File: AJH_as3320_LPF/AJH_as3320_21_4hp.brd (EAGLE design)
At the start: 19 x 106.8 mm, 58 parts, among them IC1 TL072D, IC2 CEM3320QFN24, IC3 LM4040 5.0V, IC4 TL074D, J1 PJ301_THONKICONN6, J2 PJ301_THONKICONN6, J3 PJ301_THONKICONN6, J4 PJ301_THONKICONN6

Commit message: Maded Multisheet and added input buffer
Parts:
- IC1: value TL072D -> TL074D; device linear:SO08 -> linear:SO14
- moved C11 134.6 mm to (5.59, -34.9)
- moved D2 127.7 mm to (1.27, -24.6), turned to 0 degrees
- moved R23 124.2 mm to (11.6, -24.5)
- moved D1 120.3 mm to (13.1, -17.1), turned to 0 degrees
- moved IC3 114.5 mm to (1.02, -18.0), turned to 0 degrees
- moved JP1 111.5 mm to (2.03, -7.87), turned to 0 degrees
- moved C2 107.5 mm to (0.13, -30.0), turned to 0 degrees
- moved C14 102.7 mm to (13.1, -5.21), turned to 0 degrees
- moved C13 102.5 mm to (7.49, -5.21), turned to 0 degrees
- moved C1 101.9 mm to (16.0, -24.3), turned to 0 degrees
- moved C3 87.9 mm to (5.59, -30.0)
- moved C4 81.2 mm to (11.0, -30.0)
- moved C6 74.6 mm to (0.13, -34.9), turned to 0 degrees
- moved C5 68.7 mm to (16.5, -30.0), turned to 0 degrees
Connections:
- new net N$9: IC1.10, J2.P3
- new net V+: IC1.4, IC4.4
- new net V-: IC1.11, IC4.11
- net -12V: no longer IC1.4, IC4.11
- net 12V: no longer IC1.8, IC4.4
- net LOWPASS_IN: now also IC1.8, IC1.9; no longer J2.P3
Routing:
- net 12V: track 115.0 -> 1.62 mm, vias 6 -> 0
- net -12V: track 141.4 -> 31.2 mm, vias 5 -> 3
- net N$1: track 4.84 -> 22.4 mm
- net GND: track 94.6 -> 87.2 mm
- net -5VIN: track 25.4 -> 19.6 mm
- net N$20: track 5.50 -> 0.00 mm
- net LOWPASS_OUT: track 30.4 -> 35.6 mm
- net N$6: track 5.07 -> 0.00 mm
- net N$7: track 61.9 -> 64.8 mm
- net N$8: track 4.95 -> 6.75 mm
- net LOWPASS_IN: track 31.1 -> 29.3 mm

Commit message: Updated power to op-amps
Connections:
- removed net V+: IC1.4, IC4.4
- removed net V-: IC1.11, IC4.11
- net -12V: now also IC1.11, IC4.11
- net 12V: now also IC1.4, IC4.4
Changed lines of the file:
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@@
 <contactref element="C1" pad="1"/>
 <contactref element="C13" pad="+"/>
+<contactref element="IC1" pad="4"/>
+<contactref element="IC4" pad="4"/>
+<wire x1="6.491" y1="53.792" x2="7.052" y2="77.597" width="0" layer="19" extent="1-1"/>
+<wire x1="10.672" y1="36.003" x2="6.491" y2="53.792" width="0" layer="19" extent="1-1"/>
 <wire x1="9.093" y1="-5.207" x2="10.672" y2="34.381" width="0" layer="19" extent="1-1"/>
 <wire x1="11.181" y1="-17.145" x2="9.093" y2="-5.207" width="0" layer="19" extent="1-1"/>
@@
 <contactref element="C14" pad="-"/>
 <contactref element="R23" pad="1"/>
-<wire x1="0.977" y1="-29.972" x2="0.977" y2="-34.925" width="0" layer="19" extent="1-1"/>
-<wire x1="3.17" y1="-24.638" x2="0.977" y2="-29.972" width="0" layer="19" extent="1-1"/>
-<wire x1="10.707" y1="-24.511" x2="3.17" y2="-24.638" width="0" layer="19" extent="1-1"/>
+<contactref element="IC1" pad="11"/>
+<contactref element="IC4" pad="11"/>
+<wire x1="11.691" y1="53.792" x2="12.252" y2="77.597" width="0" layer="19" extent="1-1"/>
+<wire x1="11.469" y1="37.631" x2="11.691" y2="53.792" width="0" layer="19" extent="1-1"/>
+<wire x1="11.481" y1="-5.207" x2="3.175" y2="28.2614" width="0" layer="19" extent="1-1"/>
+<wire x1="10.707" y1="-24.511" x2="11.481" y2="-5.207" width="0" layer="19" extent="1-1"/>
 <wire x1="11.899" y1="-29.972" x2="10.707" y2="-24.511" width="0" layer="19" extent="1-1"/>
-<wire x1="11.481" y1="-5.207" x2="10.707" y2="-24.511" width="0" layer="19" extent="1-1"/>
-<wire x1="3.175" y1="28.2614" x2="11.481" y2="-5.207" width="0" layer="19" extent="1-1"/>
+<wire x1="3.17" y1="-24.638" x2="10.707" y2="-24.511" width="0" layer="19" extent="1-1"/>
+<wire x1="0.977" y1="-29.972" x2="3.17" y2="-24.638" width="0" layer="19" extent="1-1"/>
+<wire x1="0.977" y1="-34.925" x2="0.977" y2="-29.972" width="0" layer="19" extent="1-1"/>
 </signal>
 <signal name="N$82">
@@
 <wire x1="6.071" y1="13.589" x2="4.674" y2="12.192" width="0.2032" layer="16"/>
 </signal>
-<signal name="V+">
-<contactref element="IC1" pad="4"/>
-<contactref element="IC4" pad="4"/>
-<wire x1="6.491" y1="53.792" x2="7.052" y2="77.597" width="0" layer="19" extent="1-1"/>
-</signal>
-<signal name="V-">
-<contactref element="IC1" pad="11"/>
-<contactref element="IC4" pad="11"/>
-<wire x1="11.691" y1="53.792" x2="12.252" y2="77.597" width="0" layer="19" extent="1-1"/>
-</signal>
 <signal name="N$6">

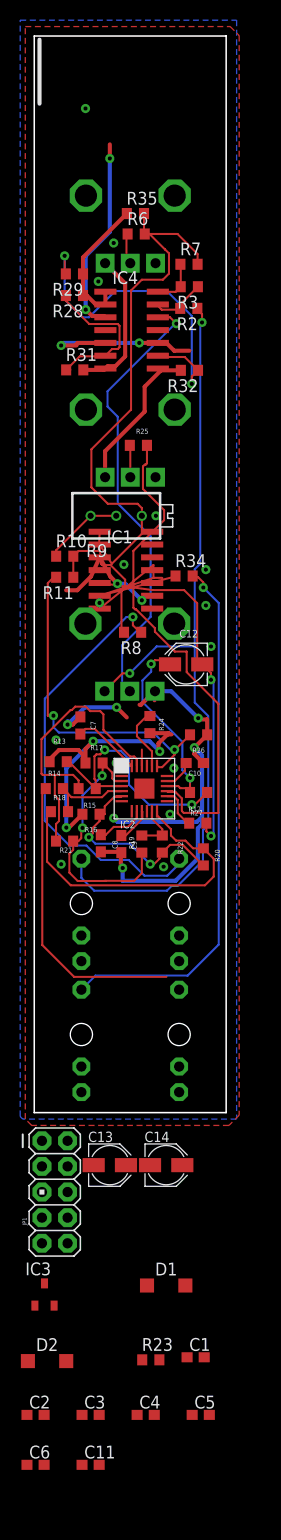
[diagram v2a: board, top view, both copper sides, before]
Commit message: First Bandpass Circuit
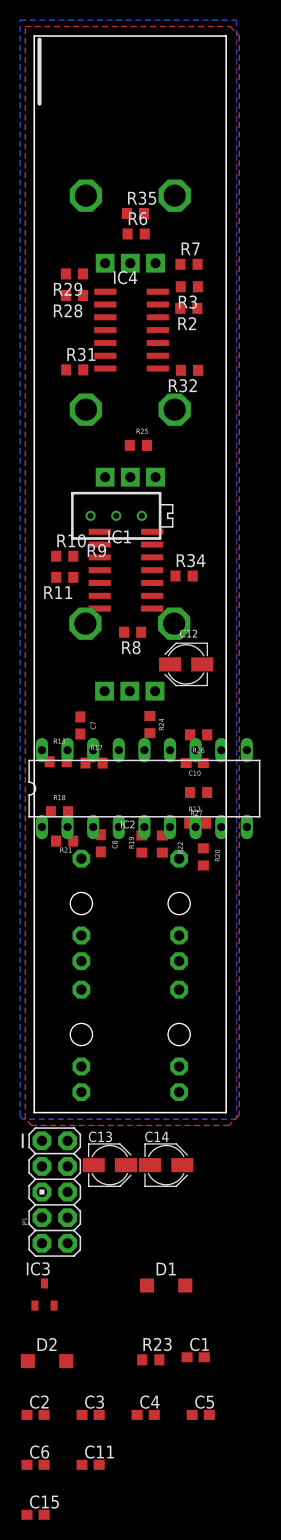
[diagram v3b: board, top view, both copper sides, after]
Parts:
- removed C9: 300pF, rcl:C0603
- removed R14, R15: 91k, rcl:R0603
- removed R16: 220k, rcl:R0603
- added C15: 300pF, rcl:C0603
- IC2: value CEM3320QFN24 -> CEM3320; device CEM:QFN24 -> CEM:DIL18
- R25: value 49.9k -> 68K
- renumbered J1 to FM_IN, J2 to SIGNALIN, J3 to V-OCT, J4 to OUTPUT
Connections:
- net LOWPASS_OUT renamed BANDPASS_OUT
- removed net LOWPASS_IN: IC1.8, IC1.9, R14.2
- removed net N$41: C8.2, IC2.P$8
- removed net N$42: C9.2, IC2.P$9
- removed net N$45: IC2.P$4, R14.1, R18.1
- removed net N$46: IC2.P$12, R18.2, R20.2
- removed net N$47: IC2.P$11, R19.1, R22.2
- removed net N$49: IC2.P$23, R15.1, R21.1
- removed net N$50: C12.+, IC2.P$16, R12.1
- removed net N$52: IC2.P$5, R16.2, R20.1, R22.1
- removed net N$53: IC2.P$2, R17.1, R19.2, R21.2
- new net BANDPASS_IN: C15.1, IC1.8, IC1.9
- new net N$14: IC2.15, R18.1, R19.1
- new net N$16: IC2.18, R13.1, R19.2, R21.2
- new net N$17: C12.+, IC2.10, R21.1
- new net N$19: C15.2, IC2.5
- new net N$23: C8.2, IC2.7, R12.1
- new net N$24: C8.1, IC2.4
- new net N$25: IC2.2, R22.1
- new net N$26: IC2.6, R20.2, R22.2
- new net N$27: IC2.1, R12.2
- net -12V: no longer R16.1
- net 12V: now also IC2.14; no longer IC2.P$22
- net FREQ_IN: now also IC2.12; no longer IC2.P$19
- net GND: now also IC2.3; no longer C8.1, C9.1, IC2.P$7
- net N$2: now also IC2.17, R17.1, R18.2, R20.1; no longer IC2.P$3, R12.2, R13.1, R15.2
- net N$40: now also IC2.16; no longer IC2.P$24
- net N$43: now also IC2.11; no longer IC2.P$17
- net N$44: now also IC2.9; no longer IC2.P$15
- net N$51: now also IC2.8; no longer IC2.P$14
- net N$54: now also IC2.13; no longer IC2.P$20
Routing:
- net GND: track 87.2 -> 0.00 mm, vias 25 -> 0
- net N$82: track 82.5 -> 0.00 mm, vias 2 -> 0
- net N$7: track 64.8 -> 0.00 mm
- net N$11: track 53.3 -> 0.00 mm, vias 1 -> 0
- net N$44: track 49.8 -> 0.00 mm
- net N$3: track 44.8 -> 0.00 mm, vias 1 -> 0
- net N$10: track 42.7 -> 0.00 mm, vias 1 -> 0
- net BANDPASS_OUT: track 35.6 -> 0.00 mm, vias 2 -> 0
- net N$13: track 34.6 -> 0.00 mm, vias 2 -> 0
- net FREQ_IN: track 33.8 -> 0.00 mm, vias 2 -> 0
- net N$46: track 32.9 -> 0.00 mm
- net -12V: track 31.2 -> 0.00 mm, vias 3 -> 0
- net N$49: track 29.8 -> 0.00 mm
- net LOWPASS_IN: track 29.3 -> 0.00 mm
- net N$2: track 25.6 -> 0.00 mm, vias 2 -> 0
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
